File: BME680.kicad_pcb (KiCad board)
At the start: 2 copper layers, 25.4 x 17.8 mm, 20 parts, among them IC1 BME680, J1 HEADER-1X770MIL, Q2 BSS138, U2 AP2112K-3.3

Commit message: update README.md + changed pin header orientation
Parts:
- J1: moved to B.Cu
- turned J1 to 90 degrees

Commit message: mosfet update
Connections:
- Q2 pad 1: 3.3V -> /SCK_3V
- Q2 pad 2: /SDI_3V -> 3.3V
- Q2 pad 3: 3.3V -> /SDI/SDA
- Q2 pad 4: /SDI/SDA -> /SDI_3V
- Q2 pad 5: /SCK_3V -> 3.3V
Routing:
- net /SCK_3V: track 11.3 -> 27.1 mm, vias 0 -> 2
- net /SDI_3V: track 13.0 -> 9.96 mm
- net /SDI/SDA: track 22.6 -> 20.6 mm
- net 3.3V: track 46.9 -> 47.8 mm

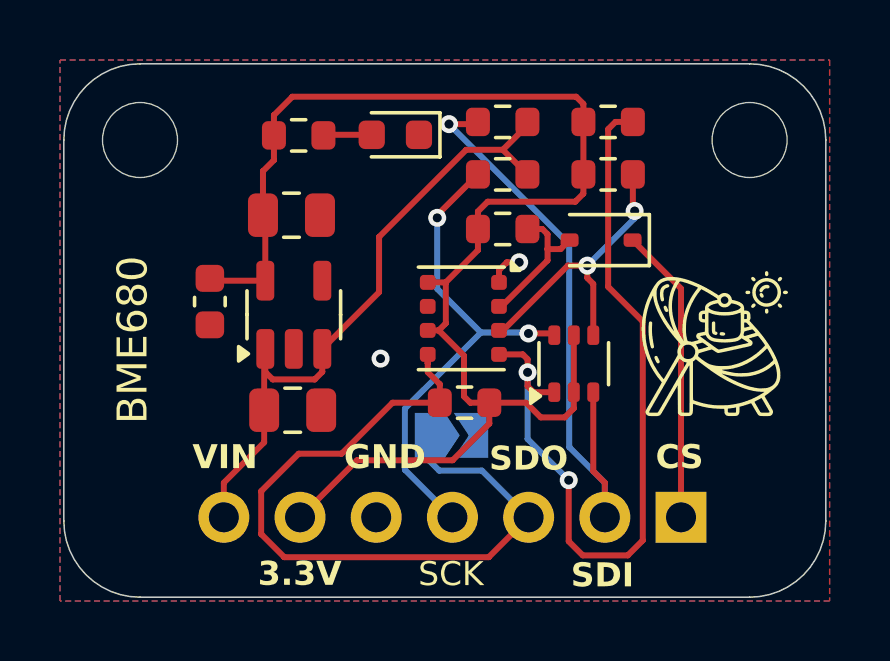
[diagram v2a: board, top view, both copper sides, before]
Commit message: DRC fix
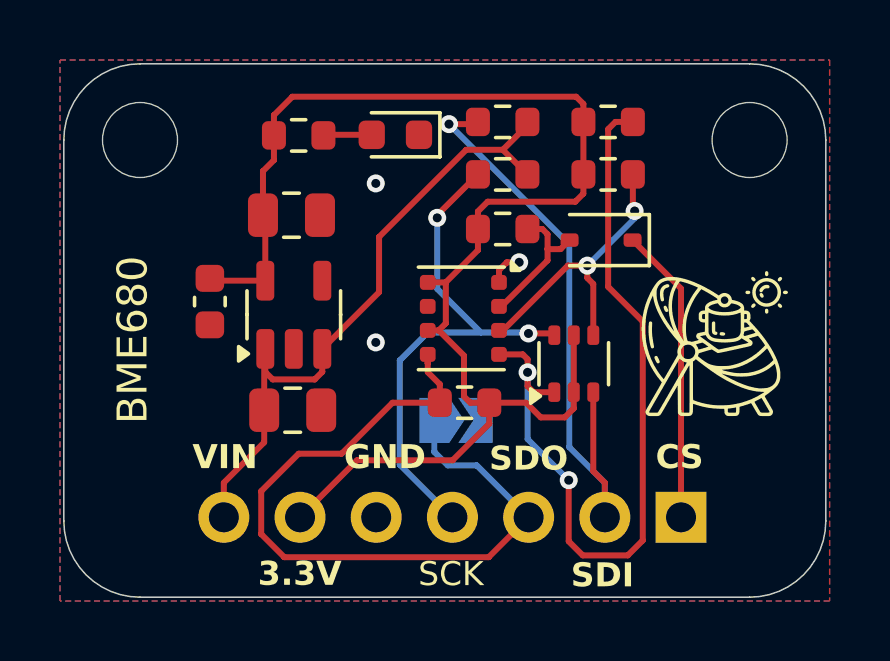
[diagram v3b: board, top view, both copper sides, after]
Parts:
- moved SJ1 0.52 mm to (148.9, 108.0)
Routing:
- net /SCK/SCL: track 16.8 -> 18.0 mm
- net GND: vias 2 -> 3
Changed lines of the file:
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@@
 	(footprint "Jumper:SolderJumper-2_P1.3mm_Open_TrianglePad1.0x1.5mm"
 		(layer "B.Cu")
-		(at 148.725 108.5)
+		(at 148.875 108)
 		(descr "SMD Solder Jumper, 1x1.5mm Triangular Pads, 0.3mm gap, open")
 		(tags "solder jumper open")
@@
 	)
 	(via
-		(at 146.36 105.94)
+		(at 146.2 105.4)
 		(size 0.6)
 		(drill 0.3)
@@
 		(net 1)
 	)
+	(via
+		(at 146.2 100.1)
+		(size 0.6)
+		(drill 0.3)
+		(layers "F.Cu" "B.Cu")
+		(free yes)
+		(net 1)
+	)
 	(segment
 		(start 142.518 103.342)
@@
 	)
 	(segment
+		(start 147 106)
+		(end 147.929 105.071)
+		(width 0.2)
+		(layer "B.Cu")
+		(net 4)
+	)
+	(segment
 		(start 148.248 103.613)
 		(end 148.248 101.248)
@@
 	)
 	(segment
-		(start 148.755 111.23)
-		(end 147.171 109.646)
-		(width 0.2)
-		(layer "B.Cu")
-		(net 4)
-	)
-	(segment
 		(start 149.706 105.071)
 		(end 148.248 103.613)
@@
 	)
 	(segment
-		(start 147.171 109.646)
-		(end 147.171 107.605)
-		(width 0.2)
-		(layer "B.Cu")
-		(net 4)
-	)
-	(segment
-		(start 147.171 107.605)
+		(start 147.929 105.071)
 		(end 149.706 105.071)
 		(width 0.2)
@@
 		(start 151.258 105.071)
 		(end 151.29 105.102)
+		(width 0.2)
+		(layer "B.Cu")
+		(net 4)
+	)
+	(segment
+		(start 148.755 111.23)
+		(end 147 109.475)
+		(width 0.2)
+		(layer "B.Cu")
+		(net 4)
+	)
+	(segment
+		(start 147 109.475)
+		(end 147 106)
 		(width 0.2)
 		(layer "B.Cu")
@@
 	)
 	(segment
-		(start 148.313 109.673)
-		(end 149.738 109.673)
+		(start 149.565 109.5)
+		(end 151.295 111.23)
 		(width 0.2)
 		(layer "B.Cu")
@@
 	)
 	(segment
-		(start 149.738 109.673)
-		(end 151.295 111.23)
+		(start 148.6 109.5)
+		(end 149.565 109.5)
 		(width 0.2)
 		(layer "B.Cu")
@@
 	)
 	(segment
-		(start 148 109.36)
-		(end 148.313 109.673)
+		(start 148.15 109.05)
+		(end 148.6 109.5)
 		(width 0.2)
 		(layer "B.Cu")
@@
 	)
 	(segment
-		(start 148 108.5)
-		(end 148 109.36)
-		(width 0.2)
-		(layer "B.Cu")
+		(start 148.15 108)
+		(end 148.15 109.05)
+		(width 0.2)
+		(layer "B.Cu")
